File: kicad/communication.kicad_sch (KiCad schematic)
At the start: 25 parts, among them J1 Screw_Terminal_01x03, J2 Screw_Terminal_01x03, J3 Conn_ARM_SWD_TagConnect_TC203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, P1 GT-USB-7014F

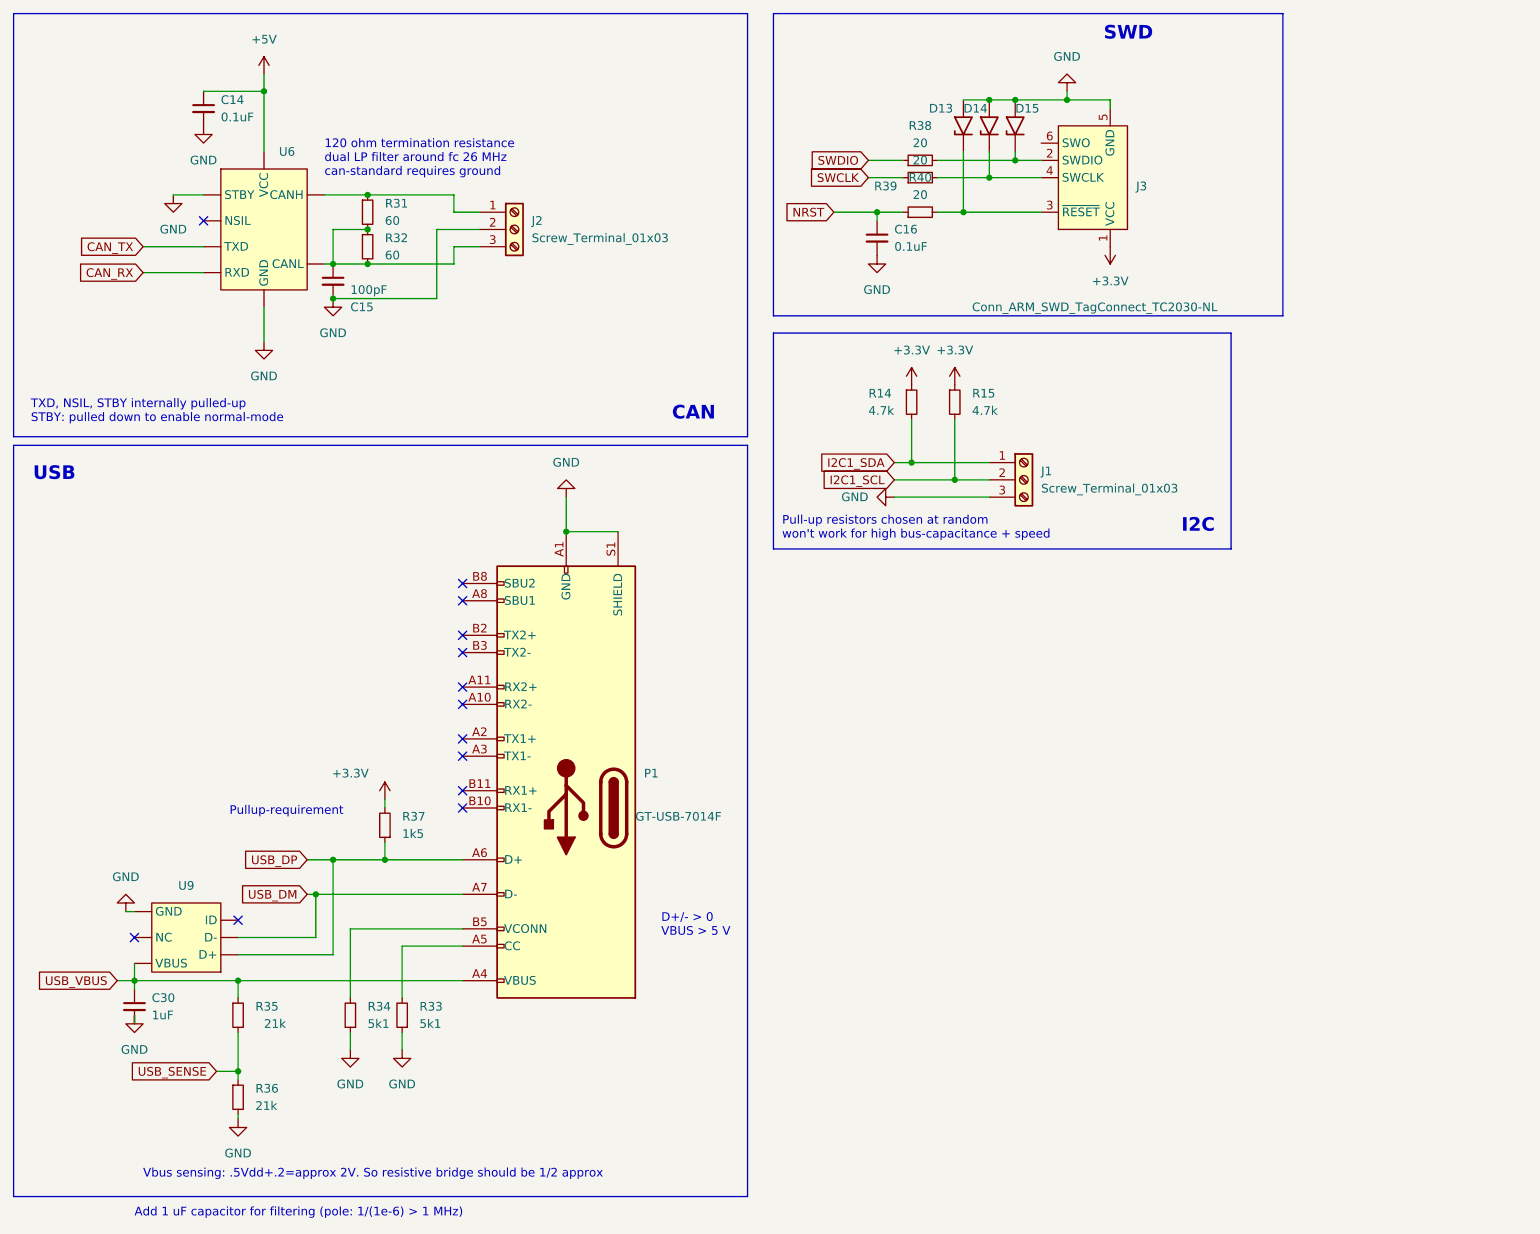
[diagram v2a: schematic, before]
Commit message: [kicad] Added resistor footprints and mfr numbers, added switching circuit for USB_DP, [simulations] Made switching circuit simulation
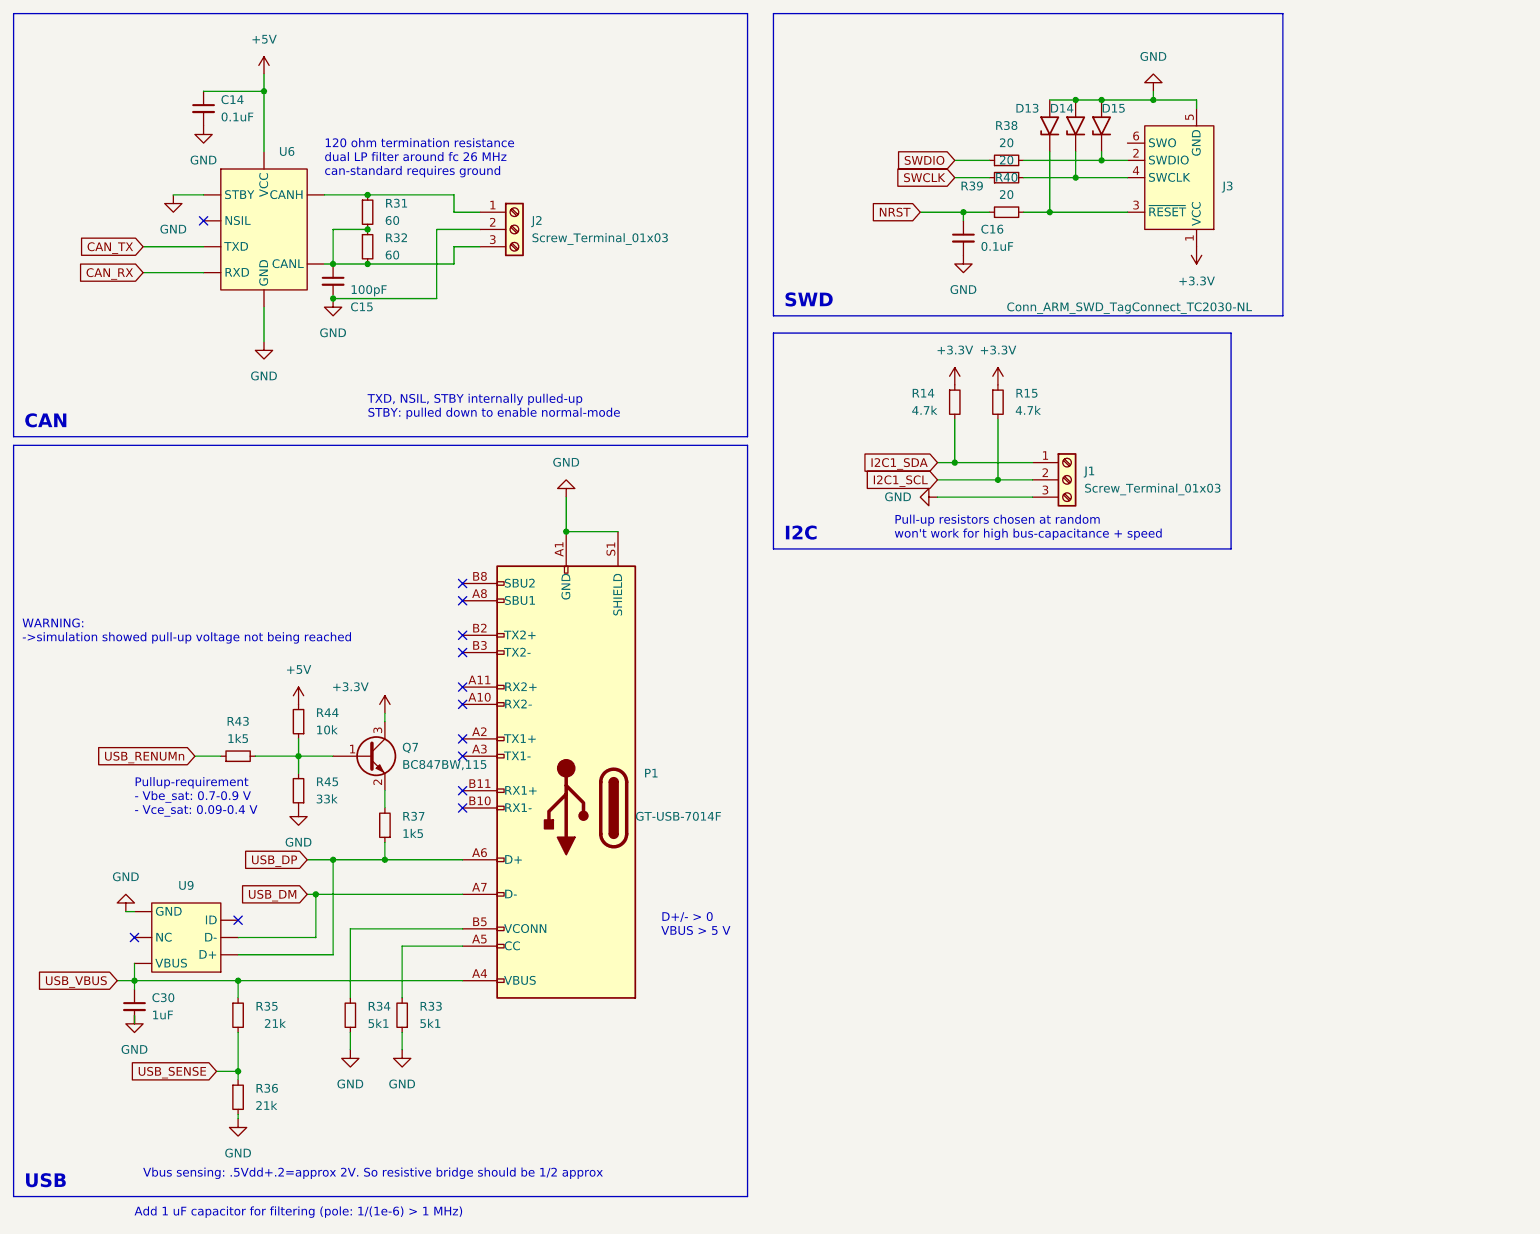
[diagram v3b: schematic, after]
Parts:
- added Q7: BC847BW,115, Package_TO_SOT_SMD:SOT-323_SC-70, symbol Transistor_BJT:BC847
- added R43: 1k5, symbol Device:R_Small
- added R44: 10k, symbol Device:R_Small
- added R45: 33k, symbol Device:R_Small
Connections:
- net +3.3V: now also Q7.3 (C); no longer R37.2
- net +5V: now also R44.2
- net GND: now also R45.1
- new net: Q7.2 (E), R37.2
- new net: Q7.1 (B), R43.2, R44.1, R45.2
- new net USB_RENUMn: R43.1
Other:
- note added: "Pullup-requirement - Vbe_sat: 0.7-0.9 V - Vce_sat: 0.09-0.4 V"
- note added: "WARNING: ->simulation showed pull-up voltage not being reached"
- note removed: "Pullup-requirement"
- moved on the sheet: C16, D13, D14, D15, J1, J3, R14, R15, R38, R39, R40

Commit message: [kicad] completed resistor and capacitor BOM, added footprints, streamlined the resistance and capacitance values | TODO: find new crystal, add footprint for CAN driver + button, check IC-footprints [simulations] adapted the simulations according to changes in the schematic [scripts] Added warning for HP 0.33 ohm resistor
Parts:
- removed P1: GT-USB-7014F, symbol Connector:USB_C_Plug
- removed R31, R32: 60, symbol Device:R_Small
- removed R38, R39, R40: 20, symbol Device:R_Small
- added J4: TYPE-C-31-M-12, Connector_USB:USB_C_Receptacle_HRO_TYPE-C-31-M-12, symbol Connector:USB_C_Receptacle_USB2.0_16P
- added R49, R50, R52: 10, Resistor_SMD:R_1206_3216Metric, symbol Device:R_Small
- added R51, R53: 56, Resistor_SMD:R_0603_1608Metric, symbol Device:R_Small
- C45: renamed from C15; footprint (none) -> Capacitor_SMD:C_0603_1608Metric; MFR.Part (none) -> CL10C101JB8NNNC; jlcpcb (none) -> C14858
- C46: renamed from C30; jlcpcb (none) -> C1848; jlpcb C1848 -> (none)
- D7: renamed from D13; value SMAJ13A -> SMAJ6.5CA; MFR.Part (none) -> SMAJ6.5CA; jlcpcb (none) -> C78404
- D8: renamed from D14; value SMAJ13A -> SMAJ6.5CA; MFR.Part (none) -> SMAJ6.5CA; jlcpcb (none) -> C78404
- D9: renamed from D15; value SMAJ13A -> SMAJ6.5CA; MFR.Part (none) -> SMAJ6.5CA; jlcpcb (none) -> C78404
- R54: renamed from R14; footprint (none) -> Resistor_SMD:R_0805_2012Metric; MFR.Part (none) -> 0805W8F4701T5E; jlcpcb (none) -> C17673
- R55: renamed from R15; footprint (none) -> Resistor_SMD:R_0805_2012Metric; MFR.Part (none) -> 0805W8F4701T5E; jlcpcb (none) -> C17673
- R56: renamed from R44; value 10k -> 12k; footprint (none) -> Resistor_SMD:R_0603_1608Metric; MFR.Part (none) -> 0603WAF1202T5E; jlcpcb (none) -> C22790
- R57: renamed from R43; value 1k5 -> 1.5k; footprint (none) -> Resistor_SMD:R_0805_2012Metric; jlcpcb (none) -> C4310
- R58: renamed from R45; footprint (none) -> Resistor_SMD:R_0603_1608Metric; jlcpcb (none) -> C4216
- R59: renamed from R37; value 1k5 -> 1.5k; footprint (none) -> Resistor_SMD:R_0805_2012Metric; jlcpcb (none) -> C4310
- R60: renamed from R35; value 21k -> 33k; footprint (none) -> Resistor_SMD:R_0603_1608Metric; jlcpcb (none) -> C4216
- R61: renamed from R34; value 5k1 -> 5.1k; footprint (none) -> Resistor_SMD:R_0805_2012Metric; MFR.Part (none) -> 0805W8F5101T5E; jlcpcb (none) -> C27834
- R62: renamed from R33; value 5k1 -> 5.1k; footprint (none) -> Resistor_SMD:R_0805_2012Metric; MFR.Part (none) -> 0805W8F5101T5E; jlcpcb (none) -> C27834
- R63: renamed from R36; value 21k -> 33k; footprint (none) -> Resistor_SMD:R_0603_1608Metric; jlcpcb (none) -> C4216
- U12: renamed from U6; JLPCB # C2671262 -> (none); MFR.Part (none) -> ATA6560-GAQW-N; jlcpcb (none) -> C2671262
- renumbered C14 to C43, C16 to C44, J3 to J1, J1 to J3, U9 to U13
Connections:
- net GND: now also J4.A1 (GND), J4.A12 (GND), J4.B1 (GND), J4.B12 (GND), J4.S1 (SHIELD)
- net NRST: now also R52.1
- net SWCLK: now also R50.1
- net SWDIO: now also R49.1
- net USB_DM: now also J4.A7 (D-), J4.B7 (D-)
- net USB_DP: now also J4.A6 (D+), J4.B6 (D+)
- net USB_VBUS: now also J4.A4 (VBUS), J4.A9 (VBUS), J4.B4 (VBUS), J4.B9 (VBUS)
- net at R61.2: now also J4.B5 (CC2)
- net at J2.1 (Pin_1), U12. (VCC): now also R51.2
- net at C45.1, J2.3 (Pin_3), U12. (VCC): now also R51.1, R53.1, R53.2
- net at R62.2: now also J4.A5 (CC1)
- net at D8.1 (A1), J1.4 (SWCLK): now also R50.2
- net at D9.1 (A1), J1.2 (SWDIO): now also R49.2
- net at D7.1 (A1), J1.3 (~{RESET}): now also R52.2
- no-connect marks 13 -> 5
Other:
- note added: "120 ohm termination resistance - dual LP filter around fc 26 MHz - can-standard requires ground (for convenience chose 51 Ohms)"
- note added: "WARNING: -> simulation showed pull-up voltage not being reached -> be sure to compare the footprint"
- note added: "Warning: Check the footprints here one more time"
- note removed: "120 ohm termination resistance dual LP filter around fc 26 MHz can-standard requires ground"
- note removed: "WARNING: ->simulation showed pull-up voltage not being reached"
- moved on the sheet: C46, Q7, R56, R57, R58, R59, R60, R61, R62, R63, U13

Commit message: [kicad] Added oscillator and relevant surrounding circuitry [scripts] Added resonator calculation
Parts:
- U13: MFR.Part (none) -> TPD4S012DRYR; jlcpcb (none) -> C96506
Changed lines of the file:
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@@
       (effects (font (size 1.27 1.27)) hide)
     )
-    (property "Datasheet" "" (at 50.165 133.985 0)
+    (property "Datasheet" "https://wmsc.lcsc.com/wmsc/upload/file/pdf/v2/lcsc/1809050016_Texas-Instruments-TPD4S012DRYR_C96506.pdf" (at 50.165 133.985 0)
       (effects (font (size 1.27 1.27)) hide)
     )
+    (property "jlcpcb" "C96506" (at 50.165 133.985 0)
+      (effects (font (size 1.27 1.27)) hide)
+    )
+    (property "MFR.Part" "TPD4S012DRYR" (at 50.165 133.985 0)
+      (effects (font (size 1.27 1.27)) hide)
+    )
